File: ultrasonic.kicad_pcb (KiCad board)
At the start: 2 copper layers, 41.4 x 35.6 mm, 23 parts, among them J1 10118192-0001LF, J2 Conn_01x03_Male, J3 Conn_01x03_Male, J4 Conn_01x03_Male, J5 Conn_01x02_Male, U1 CP2102N-A01-GQFN24, U2 ATMEGA328P-AN, U3 LM1117-ADJ

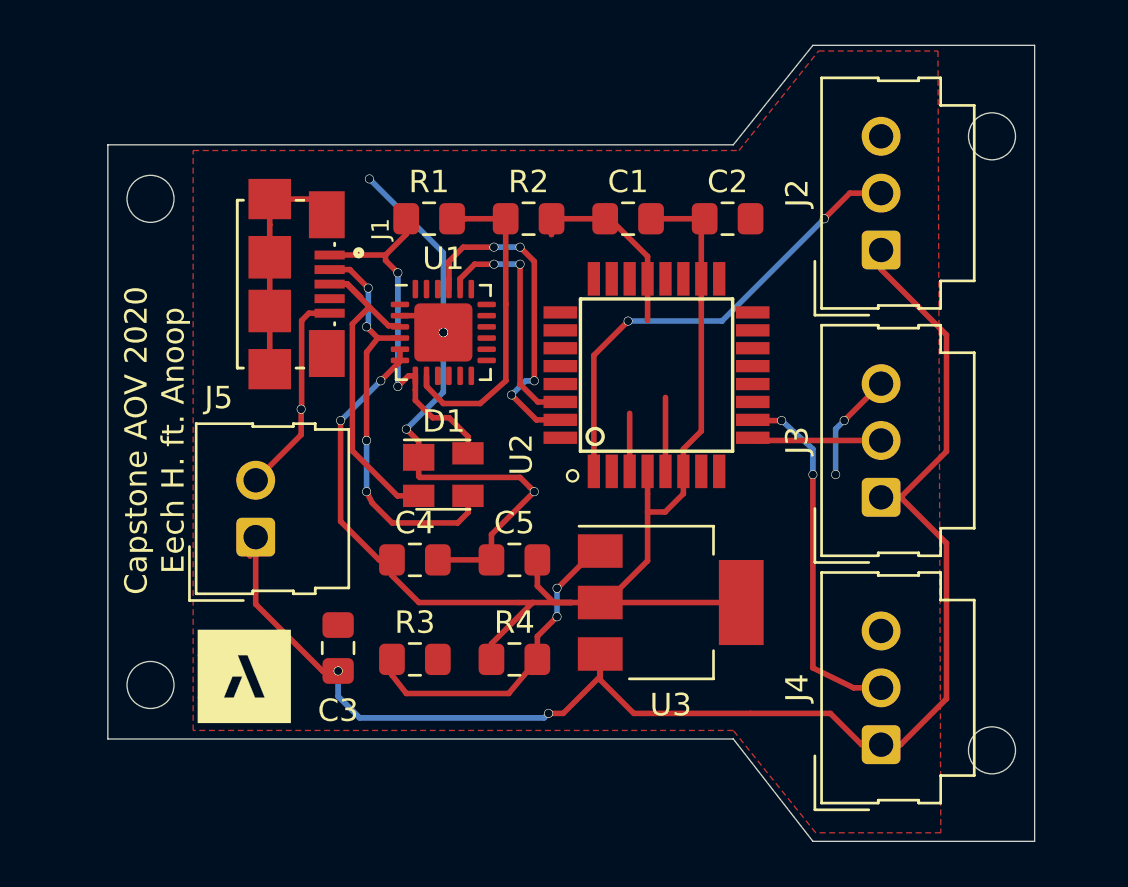
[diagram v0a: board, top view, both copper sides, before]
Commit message: Adjusted USB Connector
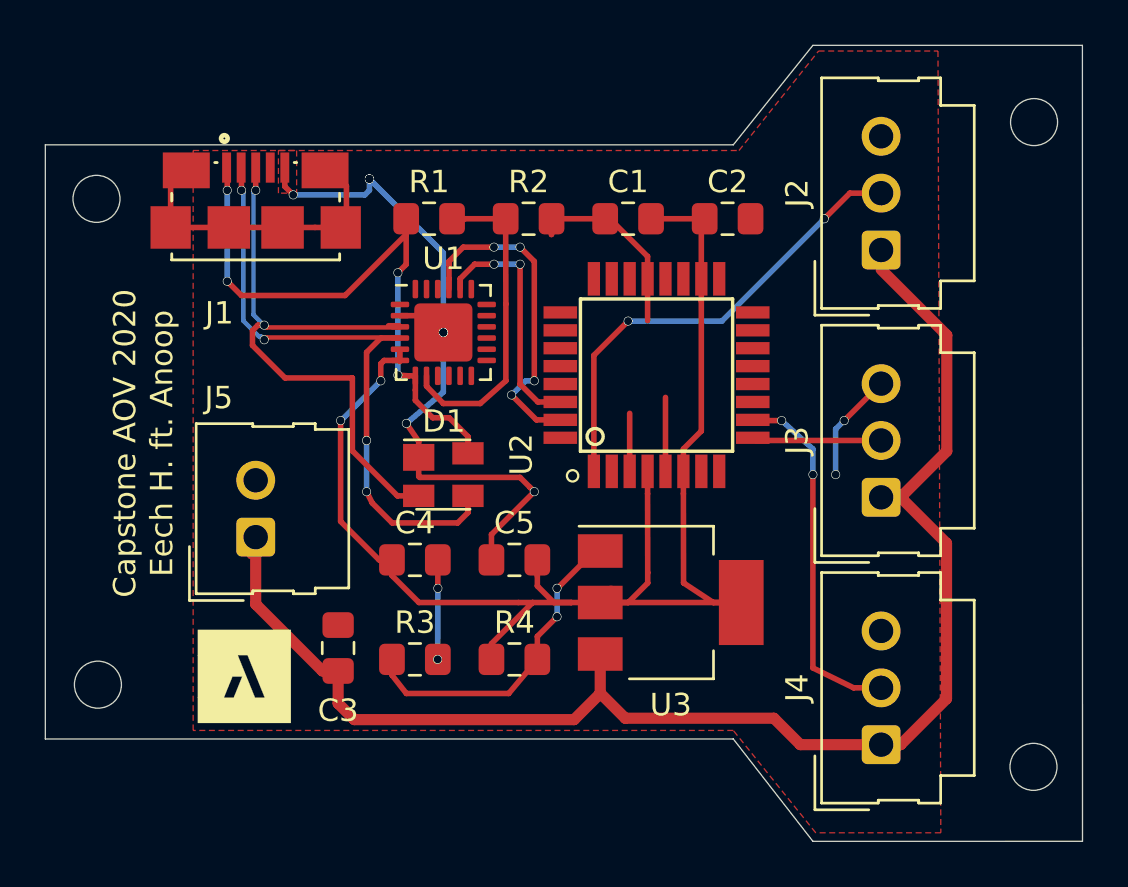
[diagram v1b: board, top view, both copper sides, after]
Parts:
- removed the REF** at (105.0, 95.6)
- removed the REF** at (105.0, 117.3)
- removed the REF** at (142.6, 92.8)
- added REF**: MountingHole_2.1mm, MountingHole:MountingHole_2.1mm, F.Cu at (102.6, 95.6)
- added REF**: MountingHole_2.1mm, MountingHole:MountingHole_2.1mm, F.Cu at (102.7, 117.3)
- added REF**: MountingHole_2.1mm, MountingHole:MountingHole_2.1mm, F.Cu at (144.5, 92.2)
- moved J1 6.17 mm to (109.7, 94.2), turned to 0 degrees
- moved REF** 2.00 mm to (144.5, 121.0)
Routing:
- net Net-(D1-Pad4): track 16.4 -> 28.0 mm, vias 2 -> 4
- net D+: track 16.1 -> 27.3 mm, vias 0 -> 2
- net D-: track 18.7 -> 28.4 mm
- net +5V: track 58.8 -> 65.7 mm
- net Net-(J1-PadSH1): track 10.4 -> 13.3 mm
- net +12V: track 66.3 -> 68.6 mm, vias 2 -> 0
- net GND: track 58.2 -> 56.3 mm, vias 8 -> 11
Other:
- board size 41.4 x 35.6 mm -> 46.3 x 35.6 mm
